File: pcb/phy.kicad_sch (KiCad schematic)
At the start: 0 parts

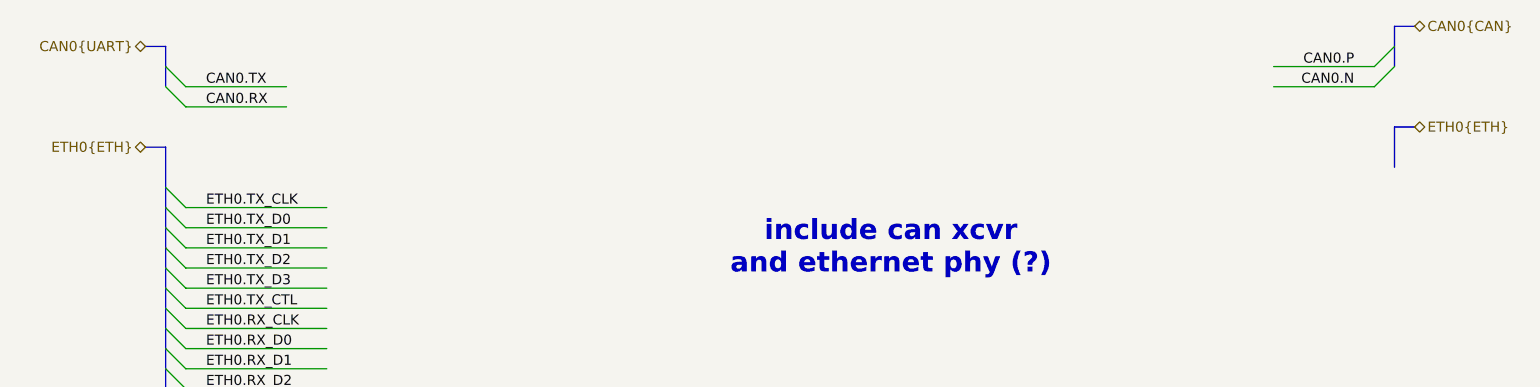
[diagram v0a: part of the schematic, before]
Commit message: edits to eth0 protocol names / bus aliases
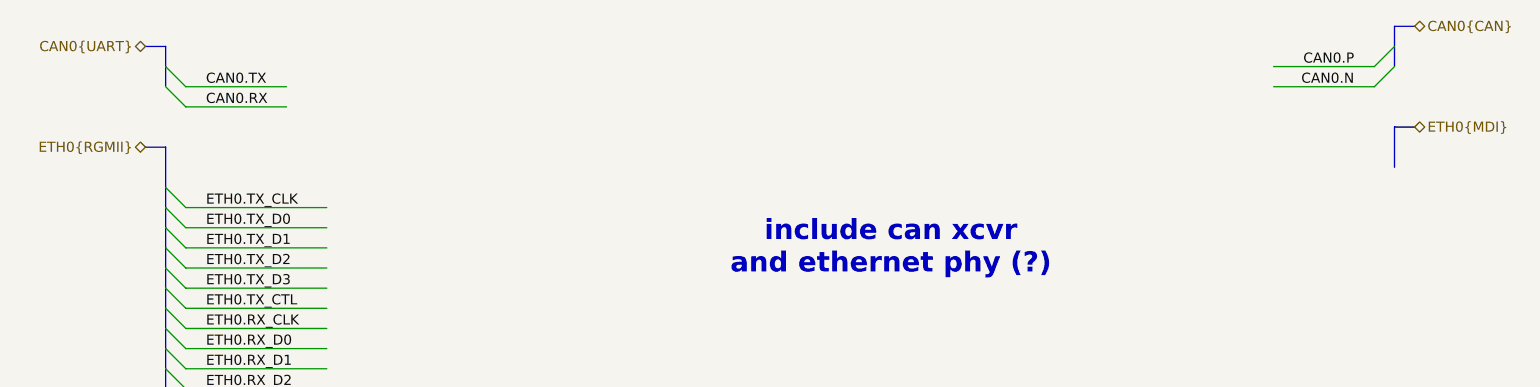
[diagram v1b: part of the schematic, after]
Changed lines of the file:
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@@
 		)
 	)
-	(hierarchical_label "ETH0{ETH}"
+	(hierarchical_label "ETH0{MDI}"
 		(shape bidirectional)
 		(at 213.36 73.66 0)
@@
 		)
 	)
-	(hierarchical_label "ETH0{ETH}"
+	(hierarchical_label "ETH0{RGMII}"
 		(shape bidirectional)
 		(at 53.34 76.2 180)

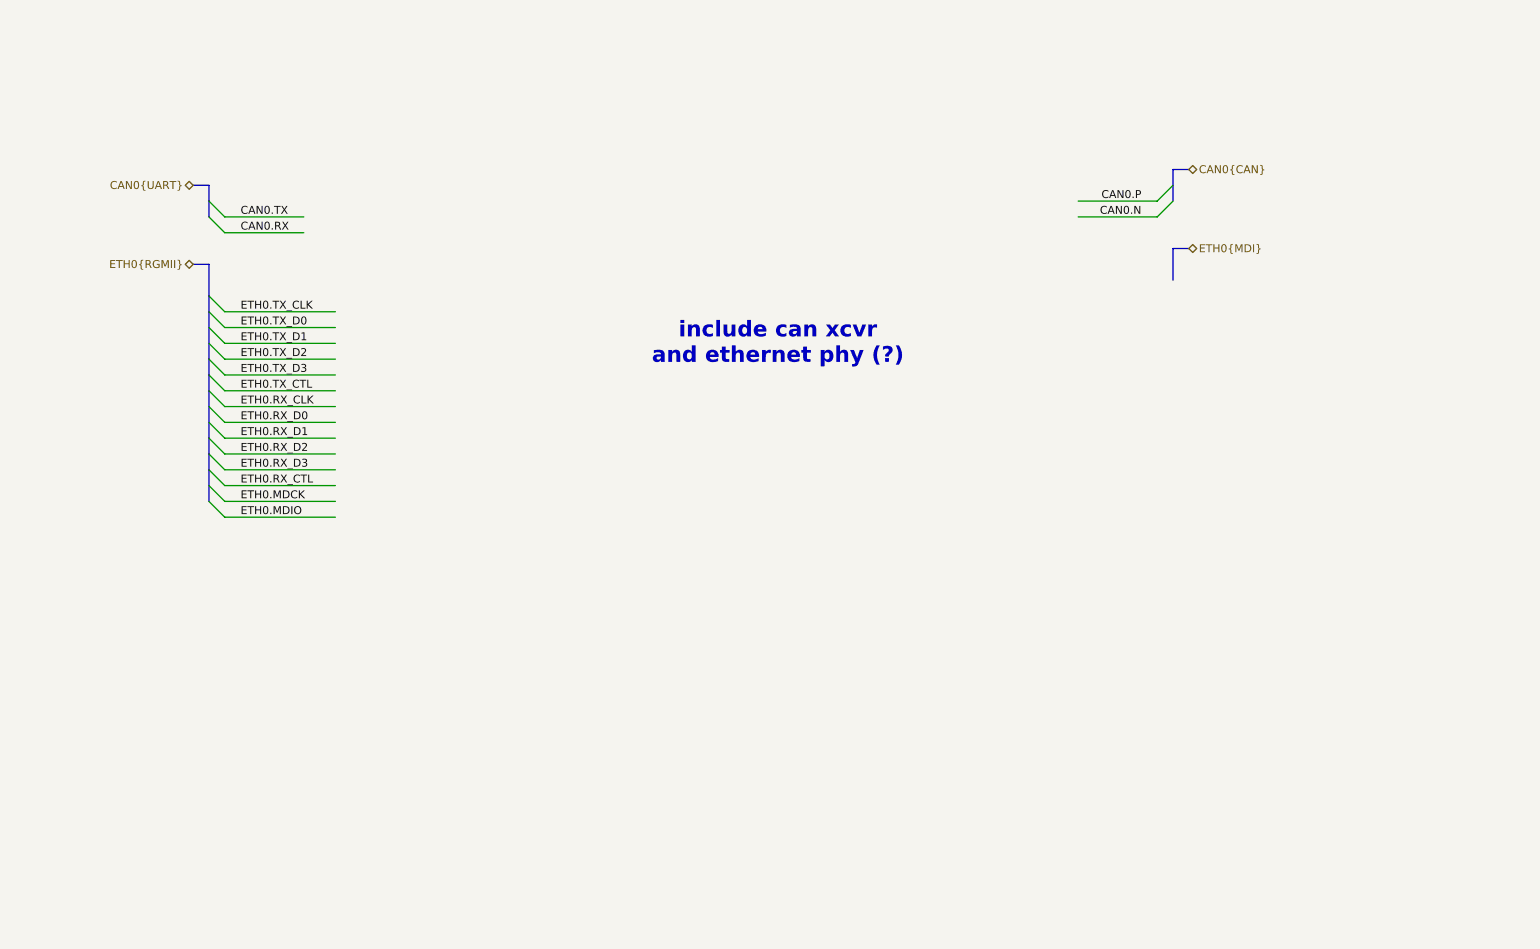
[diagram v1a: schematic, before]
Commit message: add eth phy
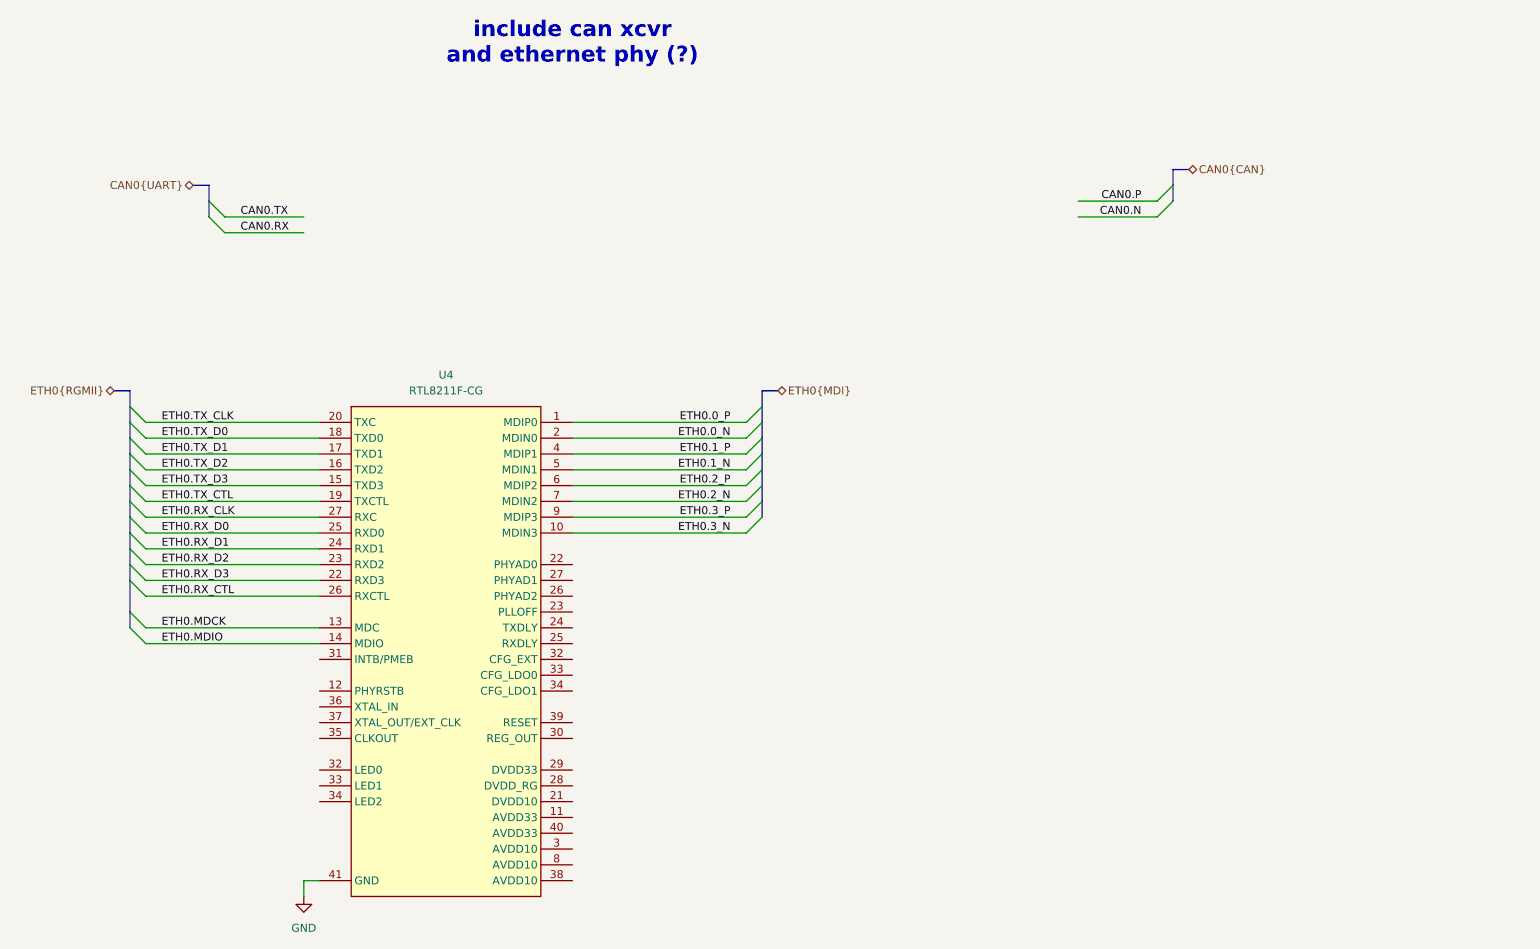
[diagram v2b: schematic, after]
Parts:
- added U4: RTL8211F-CG, Package_DFN_QFN:QFN-40-1EP_5x5mm_P0.4mm_EP3.6x3.6mm, symbol library:RTL8211F-CG
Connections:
- net ETH0.MDCK: now also U4.13 (MDC)
- net ETH0.MDIO: now also U4.14 (MDIO)
- net ETH0.RX_CLK: now also U4.27 (PHYAD1)
- net ETH0.RX_CTL: now also U4.26 (PHYAD2)
- net ETH0.RX_D0: now also U4.25 (RXDLY)
- net ETH0.RX_D1: now also U4.24 (TXDLY)
- net ETH0.RX_D2: now also U4.23 (PLLOFF)
- net ETH0.RX_D3: now also U4.22 (PHYAD0)
- net ETH0.TX_CLK: now also U4.20 (TXC)
- net ETH0.TX_CTL: now also U4.19 (TXCTL)
- net ETH0.TX_D0: now also U4.18 (TXD0)
- net ETH0.TX_D1: now also U4.17 (TXD1)
- net ETH0.TX_D2: now also U4.16 (TXD2)
- net ETH0.TX_D3: now also U4.15 (TXD3)
- new net ETH0.0_N: U4.2 (MDIN0)
- new net ETH0.0_P: U4.1 (MDIP0)
- new net ETH0.1_N: U4.5 (MDIN1)
- new net ETH0.1_P: U4.4 (MDIP1)
- new net ETH0.2_N: U4.7 (MDIN2)
- new net ETH0.2_P: U4.6 (MDIP2)
- new net ETH0.3_N: U4.10 (MDIN3)
- new net ETH0.3_P: U4.9 (MDIP3)
- new net GND: U4.41 (GND)

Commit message: phy and debug ffc conn
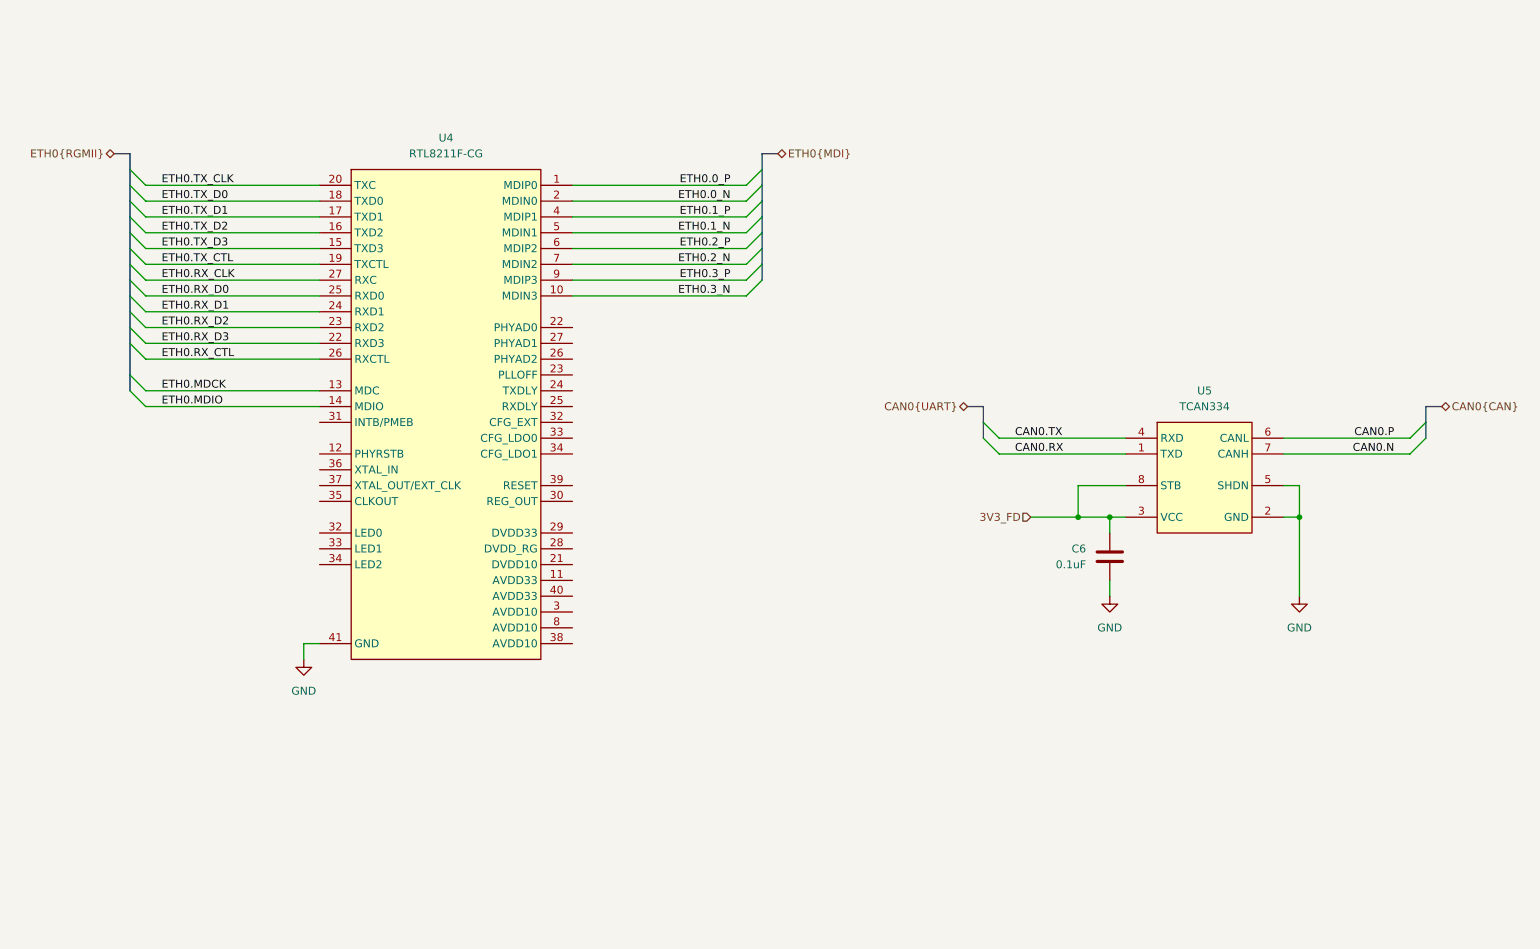
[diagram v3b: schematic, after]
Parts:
- added C6: 0.1uF, Capacitor_SMD:C_0402_1005Metric, symbol library:C
- added U5: TCAN334, Package_SO:JEITA_SOIC-8_3.9x4.9mm_P1.27mm, symbol library:TCAN334
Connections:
- net CAN0.N: now also U5.7 (CANH)
- net CAN0.P: now also U5.6 (CANL)
- net CAN0.RX: now also U5.1 (TXD)
- net CAN0.TX: now also U5.4 (RXD)
- net GND: now also C6.2, U5.2 (GND), U5.5 (SHDN)
- new net 3V3_FD: C6.1, U5.3 (VCC), U5.8 (STB)
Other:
- note removed: "include can xcvr and ethernet phy (?)"
